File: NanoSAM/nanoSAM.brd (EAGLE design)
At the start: 95.9 x 90.2 mm, 119 parts, among them J1 POWER_JACK, U1 LTC3260EMSEPBF, U2 LMV324

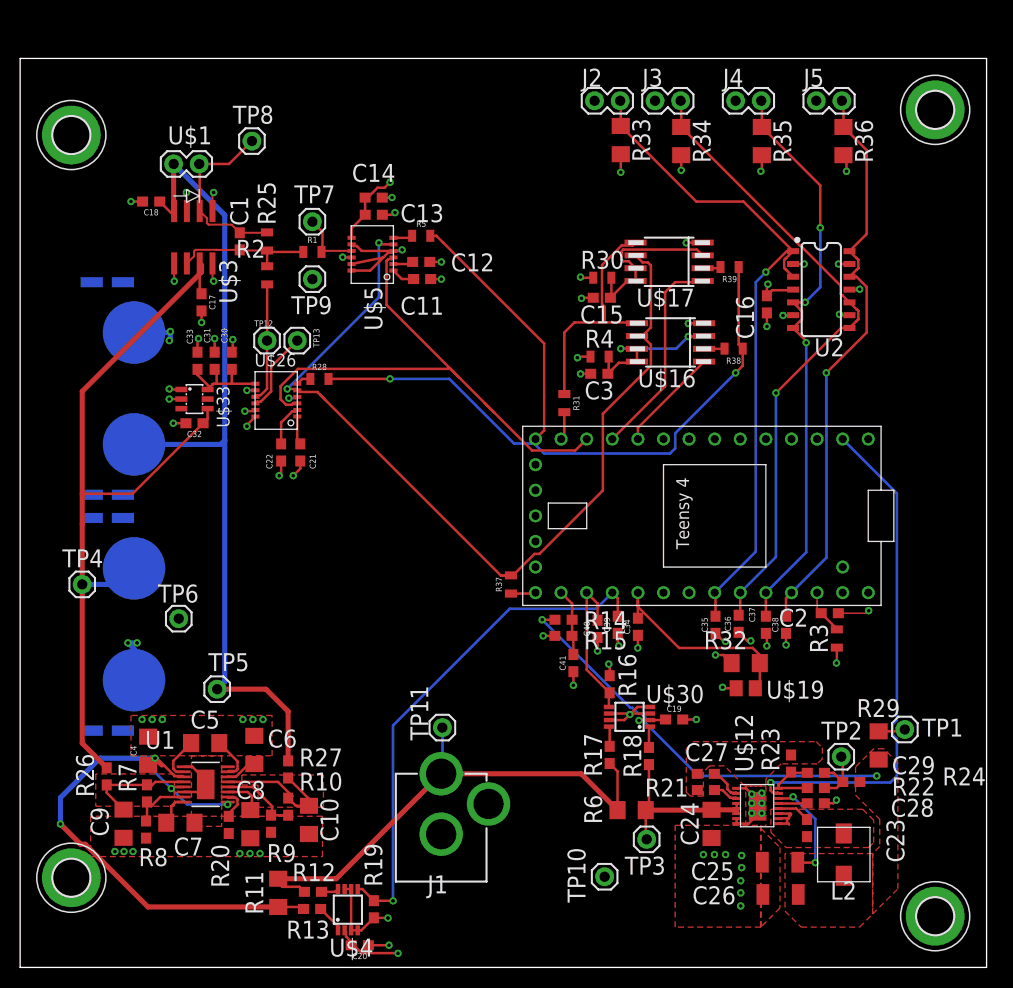
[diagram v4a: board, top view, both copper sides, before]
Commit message: Updated board dimensions to match stack plate
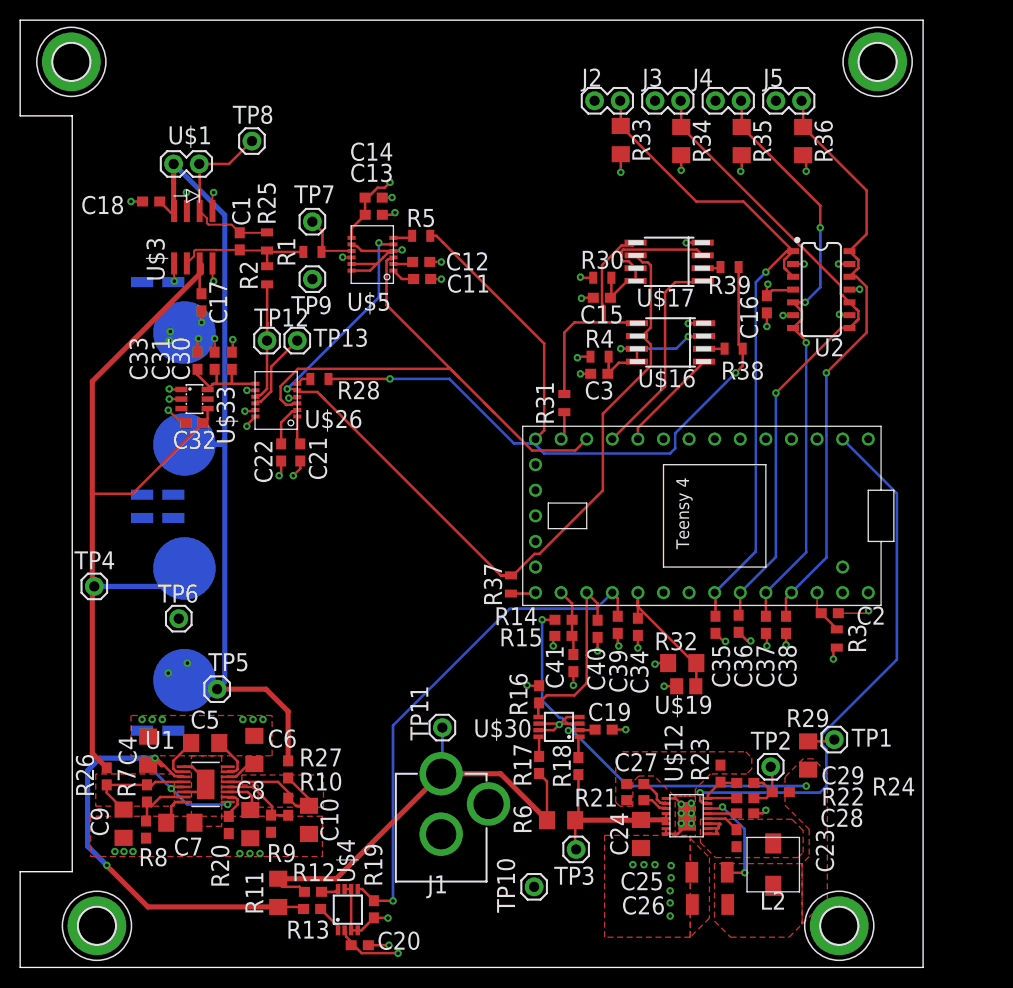
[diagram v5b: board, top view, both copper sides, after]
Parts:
- moved H3 85.0 mm to (85.1, 89.9)
- moved H2 81.5 mm to (81.3, 4.13)
- moved H1 81.0 mm to (5.08, 89.9)
- moved H4 78.5 mm to (7.62, 4.13)
- moved C19 7.07 mm to (57.9, 23.6)
- moved C27 7.07 mm to (61.0, 18.2)
- moved C23 7.07 mm to (71.1, 12.8)
- moved C24 7.07 mm to (61.6, 13.2)
- moved C25 7.07 mm to (68.4, 9.44)
- moved C26 7.07 mm to (68.5, 6.24)
- moved C28 7.07 mm to (72.0, 15.3)
- moved C29 7.07 mm to (72.0, 18.3)
- moved L2 7.07 mm to (74.7, 10.2)
- moved R16 7.07 mm to (51.5, 27.1)
- moved R17 7.07 mm to (51.5, 20.1)
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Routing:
- net HK_BRD_THRM: track 21.5 -> 14.4 mm
- net VBUS: track 52.4 -> 45.9 mm
- net -5V: track 83.2 -> 78.2 mm
- net HK_3V3_PG: track 50.5 -> 54.4 mm
- net HK_3V3_C: track 15.5 -> 19.1 mm
- net N$15: track 57.3 -> 54.8 mm
- net 5V: track 81.4 -> 83.7 mm
- net N$28: track 51.9 -> 50.0 mm
- net AGND: track 48.9 -> 47.1 mm
- net HK_INST_THRM3: track 58.1 -> 59.7 mm
- net DGND: track 75.7 -> 74.8 mm
- net +3V3: track 36.6 -> 35.7 mm
- net HK_INST_THRM2: track 58.3 -> 59.2 mm
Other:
- board size 95.9 x 90.2 mm -> 89.6 x 94 mm

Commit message: updated some values
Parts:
- C24, C4: value 4.7uF -> 4.7uF - 25V
- R14: value (none) -> 5k
- R15: value (none) -> 10k
- R29: value (none) -> 0
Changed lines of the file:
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@@
 <?xml version="1.0" encoding="utf-8"?>
 <!DOCTYPE eagle SYSTEM "eagle.dtd">
-<eagle version="9.5.2">
+<eagle version="9.3.0">
 <drawing>
 <settings>
@@
 <attribute name="VALUE" x="70.328" y="12.83" size="1.778" layer="27" font="vector" ratio="20" rot="R270" align="top-center"/>
 </element>
-<element name="C24" library="SparkFun-Capacitors" library_urn="urn:adsk.eagle:library:510" package="1206" package3d_urn="urn:adsk.eagle:package:37426/1" value="4.7uF" x="61.61" y="13.24" smashed="yes" rot="R270">
+<element name="C24" library="SparkFun-Capacitors" library_urn="urn:adsk.eagle:library:510" package="1206" package3d_urn="urn:adsk.eagle:package:37426/1" value="4.7uF - 25V" x="61.61" y="13.24" smashed="yes" rot="R270">
 <attribute name="NAME" x="58.553" y="13.24" size="1.778" layer="25" font="vector" ratio="15" rot="R270" align="bottom-center"/>
 <attribute name="PROD_ID" value="CAP-10300" x="7" y="-2" size="1.778" layer="27" rot="R270" display="off"/>
@@
 <attribute name="VALUE" x="28.97" y="6.562" size="1.778" layer="27" font="vector" ratio="20" rot="R180" align="top-center"/>
 </element>
-<element name="R14" library="SparkFun-Resistors" library_urn="urn:adsk.eagle:library:532" package="0603" package3d_urn="urn:adsk.eagle:package:39650/1" value=" " x="53.92" y="34.5" smashed="yes">
+<element name="R14" library="SparkFun-Resistors" library_urn="urn:adsk.eagle:library:532" package="0603" package3d_urn="urn:adsk.eagle:package:39650/1" value="5k" x="53.92" y="34.5" smashed="yes">
 <attribute name="NAME" x="49.22" y="33.962" size="1.778" layer="25" font="vector" ratio="15" align="bottom-center"/>
 <attribute name="PROD_ID" value=" " x="84.4" y="-29" size="1.778" layer="27" display="off"/>
 <attribute name="VALUE" x="53.92" y="33.738" size="1.778" layer="27" font="vector" ratio="20" align="top-center"/>
 </element>
-<element name="R15" library="SparkFun-Resistors" library_urn="urn:adsk.eagle:library:532" package="0603" package3d_urn="urn:adsk.eagle:package:39650/1" value=" " x="53.91" y="32.9" smashed="yes">
+<element name="R15" library="SparkFun-Resistors" library_urn="urn:adsk.eagle:library:532" package="0603" package3d_urn="urn:adsk.eagle:package:39650/1" value="10k" x="53.91" y="32.9" smashed="yes">
 <attribute name="NAME" x="49.71" y="31.862" size="1.778" layer="25" font="vector" ratio="15" align="bottom-center"/>
 <attribute name="PROD_ID" value=" " x="88.2" y="-30.6" size="1.778" layer="27" display="off"/>
@@
 <attribute name="VALUE" x="27.352" y="19.65" size="1.778" layer="27" font="vector" ratio="20" rot="R90" align="top-center"/>
 </element>
-<element name="R29" library="SparkFun-Resistors" library_urn="urn:adsk.eagle:library:532" package="1206" package3d_urn="urn:adsk.eagle:package:39654/1" value=" " x="78.19" y="21.03" smashed="yes" rot="R90">
+<element name="R29" library="SparkFun-Resistors" library_urn="urn:adsk.eagle:library:532" package="1206" package3d_urn="urn:adsk.eagle:package:39654/1" value="0" x="78.19" y="21.03" smashed="yes" rot="R90">
 <attribute name="NAME" x="78.17" y="25.628" size="1.778" layer="25" font="vector" ratio="15" rot="R180" align="bottom-center"/>
 <attribute name="PROD_ID" value=" " x="145.5" y="47.7" size="1.778" layer="27" rot="R90" display="off"/>
@@
 <attribute name="NAME" x="12.18" y="31.43" size="1.778" layer="26" rot="MR90"/>
 </element>
-<element name="C4" library="SparkFun-Capacitors" library_urn="urn:adsk.eagle:library:510" package="1206" package3d_urn="urn:adsk.eagle:package:37426/1" value="4.7uF" x="12.7" y="21.5" smashed="yes" rot="R90">
+<element name="C4" library="SparkFun-Capacitors" library_urn="urn:adsk.eagle:library:510" package="1206" package3d_urn="urn:adsk.eagle:package:37426/1" value="4.7uF - 25V" x="12.7" y="21.5" smashed="yes" rot="R90">
 <attribute name="NAME" x="11.557" y="21.5" size="1.778" layer="25" font="vector" ratio="15" rot="R90" align="bottom-center"/>
 <attribute name="PROD_ID" value="CAP-10300" x="12.7" y="21.5" size="1.778" layer="27" rot="R90" display="off"/>

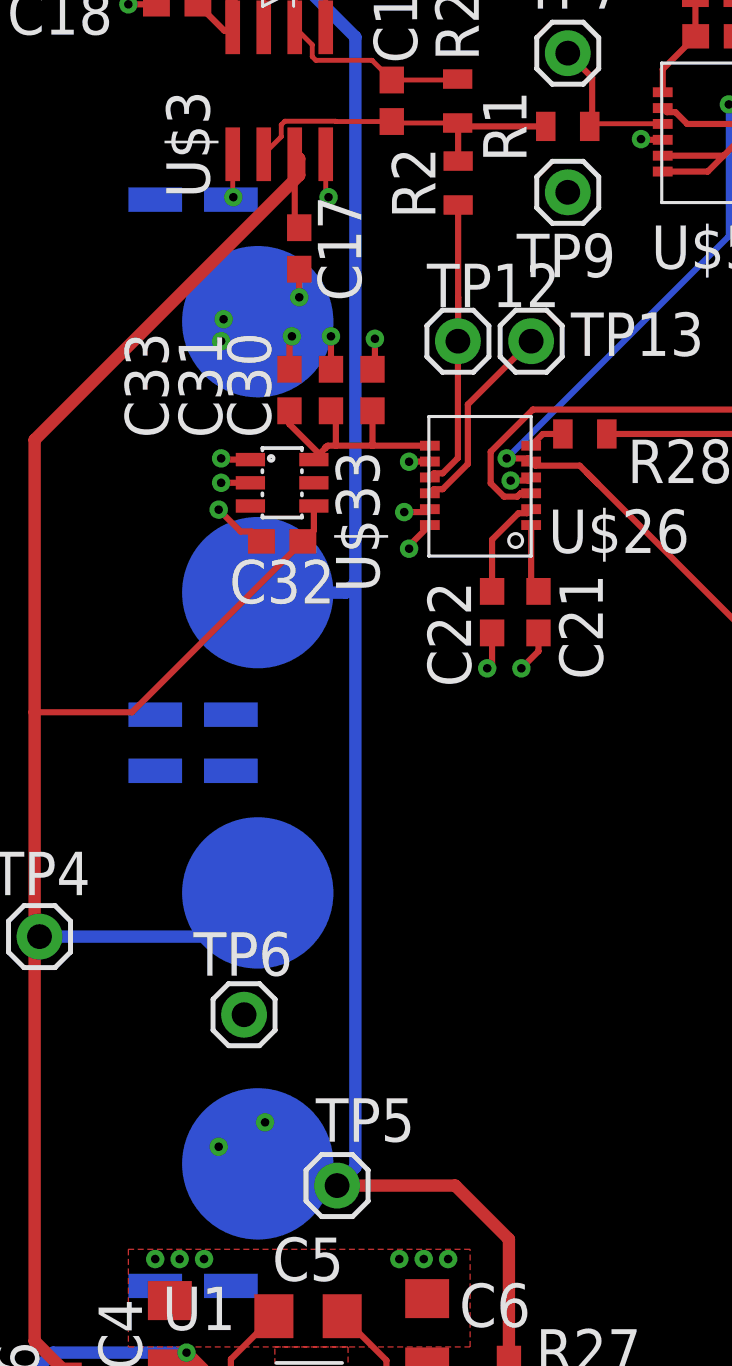
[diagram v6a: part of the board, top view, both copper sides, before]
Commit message: added manufacturing files
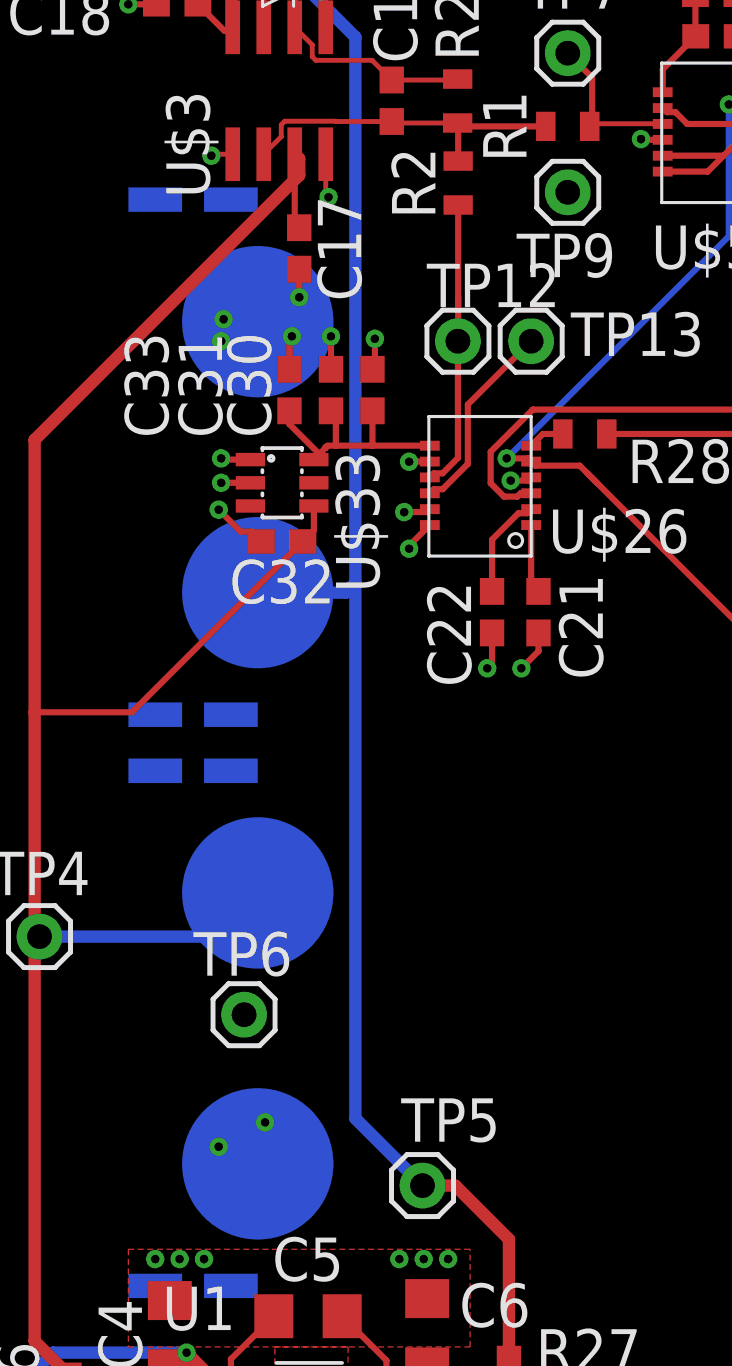
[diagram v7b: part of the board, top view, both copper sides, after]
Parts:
- moved TP5 3.50 mm to (23.1, 27.6)
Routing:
- net -5V: track 78.2 -> 75.5 mm
- net AGND: track 47.1 -> 46.2 mm
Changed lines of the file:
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@@
 <layers>
 <layer number="1" name="Top" color="4" fill="1" visible="yes" active="yes"/>
-<layer number="2" name="Route2" color="16" fill="1" visible="no" active="yes"/>
+<layer number="2" name="Route2" color="16" fill="1" visible="yes" active="yes"/>
 <layer number="3" name="Route3" color="17" fill="1" visible="no" active="no"/>
 <layer number="4" name="Route4" color="18" fill="1" visible="no" active="no"/>
@@
 <layer number="13" name="Route13" color="21" fill="1" visible="no" active="no"/>
 <layer number="14" name="Route14" color="22" fill="1" visible="no" active="no"/>
-<layer number="15" name="Route15" color="23" fill="1" visible="no" active="yes"/>
-<layer number="16" name="Bottom" color="1" fill="1" visible="no" active="yes"/>
+<layer number="15" name="Route15" color="23" fill="1" visible="yes" active="yes"/>
+<layer number="16" name="Bottom" color="1" fill="1" visible="yes" active="yes"/>
 <layer number="17" name="Pads" color="2" fill="1" visible="yes" active="yes"/>
 <layer number="18" name="Vias" color="2" fill="1" visible="yes" active="yes"/>
@@
 <attribute name="VALUE" x="6.09" y="36.286" size="0.6096" layer="27" font="vector" ratio="20" align="top-left"/>
 </element>
-<element name="TP5" library="testpoint" package="1X01" value="" x="19.55" y="27.61" smashed="yes">
-<attribute name="NAME" x="18.68" y="29.407" size="1.778" layer="25" font="vector" ratio="15"/>
-<attribute name="VALUE" x="18.28" y="26.086" size="0.6096" layer="27" font="vector" ratio="20" align="top-left"/>
+<element name="TP5" library="testpoint" package="1X01" value="" x="23.05" y="27.61" smashed="yes">
+<attribute name="NAME" x="22.18" y="29.407" size="1.778" layer="25" font="vector" ratio="15"/>
+<attribute name="VALUE" x="21.78" y="26.086" size="0.6096" layer="27" font="vector" ratio="20" align="top-left"/>
 </element>
 <element name="TP6" library="testpoint" package="1X01" value="" x="15.74" y="34.61" smashed="yes">
@@
 <vertex x="0" y="0"/>
 <vertex x="34" y="0"/>
+<vertex x="34" y="16"/>
+<vertex x="37" y="16"/>
+<vertex x="37" y="21"/>
+<vertex x="34" y="21"/>
 <vertex x="34" y="94"/>
 </polygon>
@@
 <wire x1="16.545" y1="75.06" x2="16.545" y2="76.855" width="0.2" layer="1"/>
 <wire x1="16.545" y1="76.855" x2="16.5" y2="76.9" width="0.2" layer="1"/>
-<via x="15.3" y="68.1" extent="1-16" drill="0.35"/>
+<via x="14.4" y="69.8" extent="1-16" drill="0.35"/>
 <via x="19.2" y="76.9" extent="1-16" drill="0.35"/>
 <via x="19.2" y="68.1" extent="1-16" drill="0.35"/>
-<wire x1="15.275" y1="69.86" x2="15.275" y2="68.125" width="0.2" layer="1"/>
-<wire x1="15.275" y1="68.125" x2="15.3" y2="68.1" width="0.2" layer="1"/>
+<wire x1="15.275" y1="69.86" x2="14.46" y2="69.86" width="0.2" layer="1"/>
+<wire x1="14.46" y1="69.86" x2="14.4" y2="69.8" width="0.2" layer="1"/>
 <wire x1="19.085" y1="69.86" x2="19.085" y2="68.215" width="0.2" layer="1"/>
 <wire x1="19.085" y1="68.215" x2="19.2" y2="68.1" width="0.2" layer="1"/>
@@
 <contactref element="U$21" pad="P$1"/>
 <via x="16.6" y="30.2" extent="1-16" drill="0.35"/>
-<polygon width="0.254" layer="2">
-<vertex x="32" y="17"/>
-<vertex x="32" y="15"/>
-<vertex x="36.8" y="15"/>
-<vertex x="36.8" y="17"/>
-</polygon>
 <contactref element="C4" pad="2"/>
 <wire x1="32.89" y1="70.45" x2="32.0294" y2="70.45" width="0.254" layer="1"/>
@@
 <contactref element="R27" pad="2"/>
 <wire x1="26.59" y1="20.5" x2="26.59" y2="25.41" width="0.508" layer="1"/>
-<wire x1="24.39" y1="27.61" x2="19.55" y2="27.61" width="0.508" layer="1"/>
+<wire x1="24.39" y1="27.61" x2="23.05" y2="27.61" width="0.508" layer="1"/>
 <wire x1="26.59" y1="25.41" x2="24.39" y2="27.61" width="0.508" layer="1"/>
 <wire x1="15.23" y1="79.73" x2="20.3" y2="74.66" width="0.508" layer="16"/>
-<wire x1="19.55" y1="27.61" x2="20.3" y2="28.36" width="0.508" layer="16"/>
+<wire x1="23.05" y1="27.61" x2="20.3" y2="30.36" width="0.508" layer="16"/>
 <wire x1="20.3" y1="74.66" x2="20.3" y2="52.3" width="0.508" layer="16"/>
 <contactref element="U$1" pad="2"/>
 <contactref element="U$3" pad="4"/>
-<wire x1="20.3" y1="52.3" x2="20.3" y2="28.36" width="0.508" layer="16"/>
+<wire x1="20.3" y1="52.3" x2="20.3" y2="30.36" width="0.508" layer="16"/>
 <wire x1="15.275" y1="75.06" x2="15.23" y2="75.105" width="0.2" layer="1"/>
 <wire x1="15.23" y1="75.105" x2="15.23" y2="79.73" width="0.508" layer="1"/>
